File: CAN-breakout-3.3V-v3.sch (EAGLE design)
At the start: 11 parts, among them IC1 TJA1049

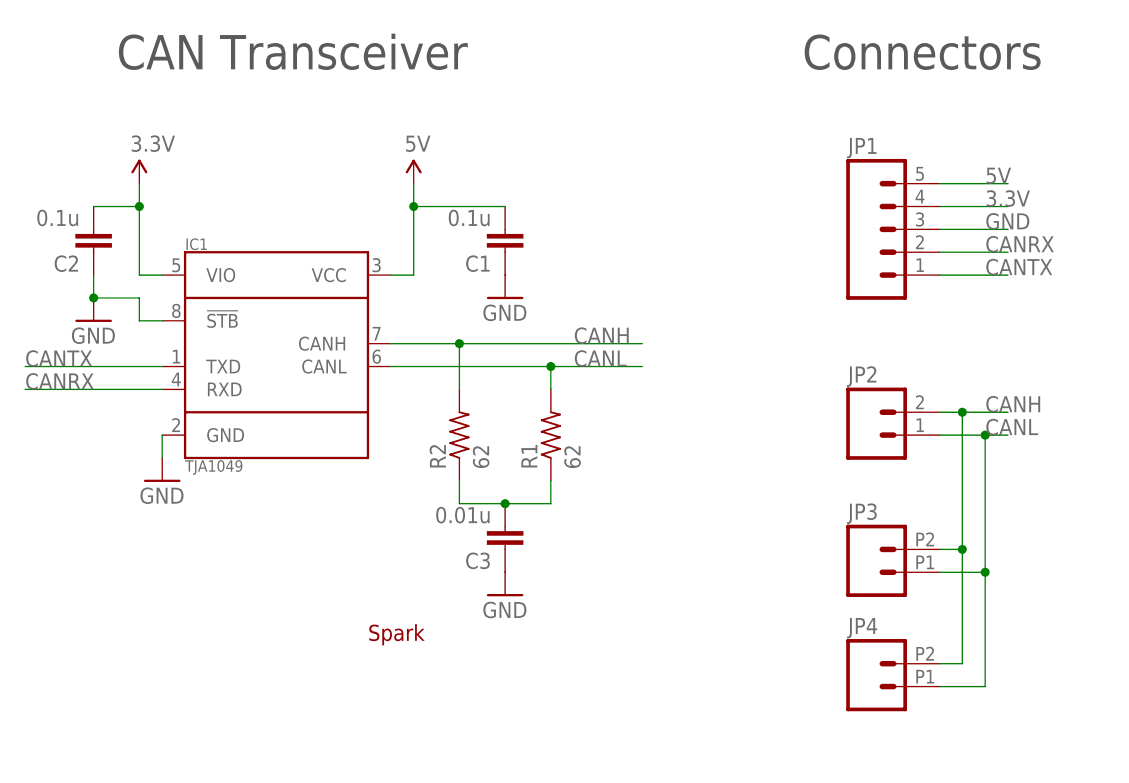
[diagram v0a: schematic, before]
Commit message: Add 3.3V variant
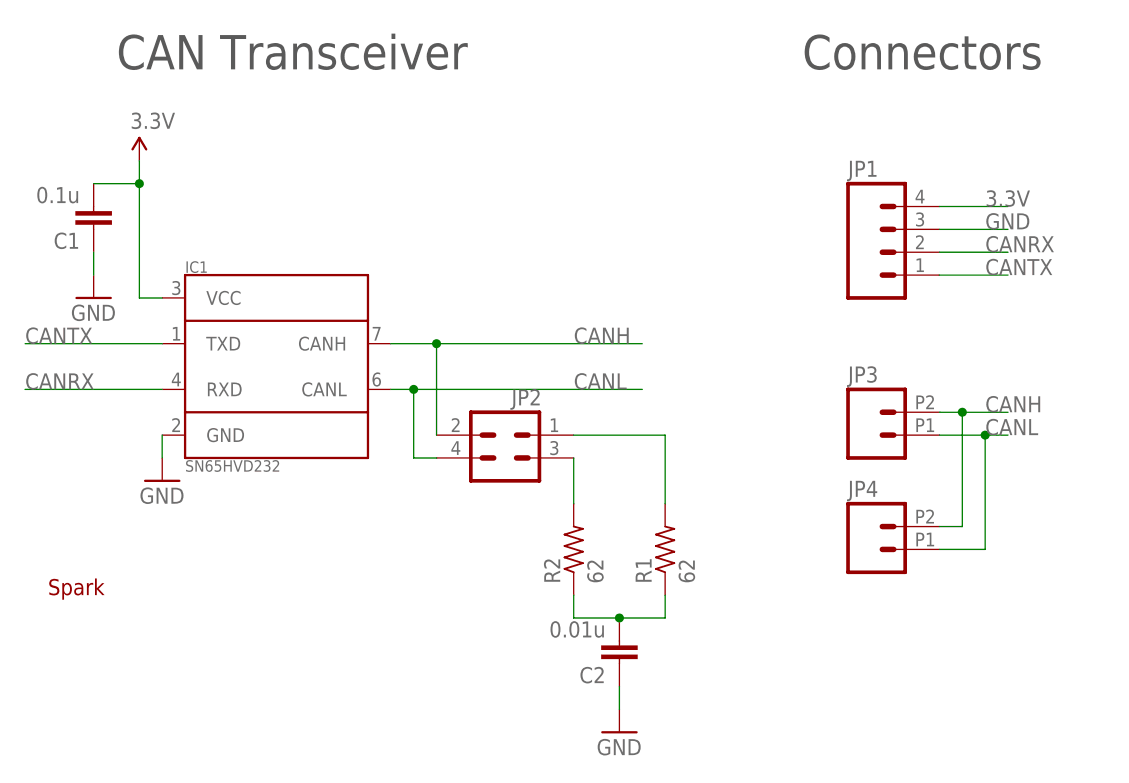
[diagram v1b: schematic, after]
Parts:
- removed C3: 0.01u, rcl:C-EUC1206
- C2: value 0.1u -> 0.01u; PARTNO 12065C104KAT2A -> 12065C103KAT2A
- IC1: value TJA1049 -> SN65HVD232; device CAN:TJA1049 -> CAN:SN65HVD232
- JP1: device SparkFun-Connectors:M05PTH -> SparkFun-Connectors:M04PTH
- JP2: device SparkFun-Connectors:M02PTH -> CAN:M02X2; PARTNO PREC002SAAN-RC -> (none)
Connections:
- removed net 5V: C1.2, IC1.VCC, JP1.5
- new net N$1: JP2.1, R1.2
- new net N$10: JP2.3, R2.2
- net 3.3V: now also C1.2, IC1.VCC; no longer C2.2, IC1.VIO
- net CANH: no longer R2.2
- net CANL: now also JP2.4; no longer JP2.1, R1.2
- net GND: no longer C3.1, IC1.!STB
- net N$7: now also C2.2; no longer C3.2
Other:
- moved on the sheet: C1, C2, JP3, JP4, R1, R2

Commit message: Create Gerbers
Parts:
- removed U$3: SPARK_LOGO2, Spark:SPARK_LOGO2
- IC1: PARTNO TJA1049T-118 -> SN65HVD232DR
- JP1: PARTNO PREC005SAAN-RC -> PREC004SAAN-RC
- JP2: PARTNO (none) -> PREC002DAAN-RC
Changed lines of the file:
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@@
 <grid distance="0.1" unitdist="inch" unit="inch" style="lines" multiple="1" display="no" altdistance="0.01" altunitdist="inch" altunit="inch"/>
 <layers>
-<layer number="1" name="Top" color="4" fill="1" visible="yes" active="no"/>
-<layer number="2" name="Route2" color="1" fill="3" visible="yes" active="no"/>
-<layer number="3" name="Route3" color="4" fill="3" visible="yes" active="no"/>
-<layer number="4" name="Route4" color="1" fill="4" visible="yes" active="no"/>
-<layer number="5" name="Route5" color="4" fill="4" visible="yes" active="no"/>
-<layer number="6" name="Route6" color="1" fill="8" visible="yes" active="no"/>
-<layer number="7" name="Route7" color="4" fill="8" visible="yes" active="no"/>
-<layer number="8" name="Route8" color="1" fill="2" visible="yes" active="no"/>
-<layer number="9" name="Route9" color="4" fill="2" visible="yes" active="no"/>
-<layer number="10" name="Route10" color="1" fill="7" visible="yes" active="no"/>
-<layer number="11" name="Route11" color="4" fill="7" visible="yes" active="no"/>
-<layer number="12" name="Route12" color="1" fill="5" visible="yes" active="no"/>
-<layer number="13" name="Route13" color="4" fill="5" visible="yes" active="no"/>
-<layer number="14" name="Route14" color="1" fill="6" visible="yes" active="no"/>
-<layer number="15" name="Route15" color="4" fill="6" visible="yes" active="no"/>
-<layer number="16" name="Bottom" color="1" fill="1" visible="yes" active="no"/>
-<layer number="17" name="Pads" color="2" fill="1" visible="yes" active="no"/>
-<layer number="18" name="Vias" color="2" fill="1" visible="yes" active="no"/>
-<layer number="19" name="Unrouted" color="6" fill="1" visible="yes" active="no"/>
-<layer number="20" name="Dimension" color="15" fill="1" visible="yes" active="no"/>
-<layer number="21" name="tPlace" color="7" fill="1" visible="yes" active="no"/>
-<layer number="22" name="bPlace" color="7" fill="1" visible="yes" active="no"/>
-<layer number="23" name="tOrigins" color="15" fill="1" visible="yes" active="no"/>
-<layer number="24" name="bOrigins" color="15" fill="1" visible="yes" active="no"/>
-<layer number="25" name="tNames" color="7" fill="1" visible="yes" active="no"/>
-<layer number="26" name="bNames" color="7" fill="1" visible="yes" active="no"/>
-<layer number="27" name="tValues" color="7" fill="1" visible="yes" active="no"/>
-<layer number="28" name="bValues" color="7" fill="1" visible="yes" active="no"/>
+<layer number="1" name="Top" color="4" fill="1" visible="no" active="no"/>
+<layer number="2" name="Route2" color="1" fill="3" visible="no" active="no"/>
+<layer number="3" name="Route3" color="4" fill="3" visible="no" active="no"/>
+<layer number="4" name="Route4" color="1" fill="4" visible="no" active="no"/>
+<layer number="5" name="Route5" color="4" fill="4" visible="no" active="no"/>
+<layer number="6" name="Route6" color="1" fill="8" visible="no" active="no"/>
+<layer number="7" name="Route7" color="4" fill="8" visible="no" active="no"/>
+<layer number="8" name="Route8" color="1" fill="2" visible="no" active="no"/>
+<layer number="9" name="Route9" color="4" fill="2" visible="no" active="no"/>
+<layer number="10" name="Route10" color="1" fill="7" visible="no" active="no"/>
+<layer number="11" name="Route11" color="4" fill="7" visible="no" active="no"/>
+<layer number="12" name="Route12" color="1" fill="5" visible="no" active="no"/>
+<layer number="13" name="Route13" color="4" fill="5" visible="no" active="no"/>
+<layer number="14" name="Route14" color="1" fill="6" visible="no" active="no"/>
+<layer number="15" name="Route15" color="4" fill="6" visible="no" active="no"/>
+<layer number="16" name="Bottom" color="1" fill="1" visible="no" active="no"/>
+<layer number="17" name="Pads" color="2" fill="1" visible="no" active="no"/>
+<layer number="18" name="Vias" color="2" fill="1" visible="no" active="no"/>
+<layer number="19" name="Unrouted" color="6" fill="1" visible="no" active="no"/>
+<layer number="20" name="Dimension" color="15" fill="1" visible="no" active="no"/>
+<layer number="21" name="tPlace" color="7" fill="1" visible="no" active="no"/>
+<layer number="22" name="bPlace" color="7" fill="1" visible="no" active="no"/>
+<layer number="23" name="tOrigins" color="15" fill="1" visible="no" active="no"/>
+<layer number="24" name="bOrigins" color="15" fill="1" visible="no" active="no"/>
+<layer number="25" name="tNames" color="7" fill="1" visible="no" active="no"/>
+<layer number="26" name="bNames" color="7" fill="1" visible="no" active="no"/>
+<layer number="27" name="tValues" color="7" fill="1" visible="no" active="no"/>
+<layer number="28" name="bValues" color="7" fill="1" visible="no" active="no"/>
 <layer number="29" name="tStop" color="7" fill="3" visible="no" active="no"/>
 <layer number="30" name="bStop" color="7" fill="6" visible="no" active="no"/>
@@
 <layer number="35" name="tGlue" color="7" fill="4" visible="no" active="no"/>
 <layer number="36" name="bGlue" color="7" fill="5" visible="no" active="no"/>
-<layer number="37" name="tTest" color="7" fill="1" visible="yes" active="no"/>
-<layer number="38" name="bTest" color="7" fill="1" visible="yes" active="no"/>
+<layer number="37" name="tTest" color="7" fill="1" visible="no" active="no"/>
+<layer number="38" name="bTest" color="7" fill="1" visible="no" active="no"/>
 <layer number="39" name="tKeepout" color="4" fill="11" visible="no" active="no"/>
 <layer number="40" name="bKeepout" color="1" fill="11" visible="no" active="no"/>
@@
 <layer number="44" name="Drills" color="7" fill="1" visible="no" active="no"/>
 <layer number="45" name="Holes" color="7" fill="1" visible="no" active="no"/>
-<layer number="46" name="Milling" color="3" fill="1" visible="yes" active="no"/>
-<layer number="47" name="Measures" color="7" fill="1" visible="yes" active="no"/>
-<layer number="48" name="Document" color="7" fill="1" visible="yes" active="no"/>
-<layer number="49" name="Reference" color="7" fill="1" visible="yes" active="no"/>
-<layer number="50" name="dxf" color="7" fill="1" visible="yes" active="no"/>
-<layer number="51" name="tDocu" color="7" fill="1" visible="yes" active="no"/>
-<layer number="52" name="bDocu" color="7" fill="1" visible="yes" active="no"/>
-<layer number="53" name="tGND_GNDA" color="7" fill="9" visible="yes" active="no"/>
-<layer number="54" name="bGND_GNDA" color="1" fill="9" visible="yes" active="no"/>
-<layer number="56" name="wert" color="7" fill="1" visible="yes" active="no"/>
-<layer number="57" name="tCAD" color="7" fill="1" visible="yes" active="no"/>
-<layer number="59" name="tCarbon" color="7" fill="1" visible="yes" active="no"/>
-<layer number="60" name="bCarbon" color="7" fill="1" visible="yes" active="no"/>
+<layer number="46" name="Milling" color="3" fill="1" visible="no" active="no"/>
+<layer number="47" name="Measures" color="7" fill="1" visible="no" active="no"/>
+<layer number="48" name="Document" color="7" fill="1" visible="no" active="no"/>
+<layer number="49" name="Reference" color="7" fill="1" visible="no" active="no"/>
+<layer number="50" name="dxf" color="7" fill="1" visible="no" active="no"/>
+<layer number="51" name="tDocu" color="7" fill="1" visible="no" active="no"/>
+<layer number="52" name="bDocu" color="7" fill="1" visible="no" active="no"/>
+<layer number="53" name="tGND_GNDA" color="7" fill="9" visible="no" active="no"/>
+<layer number="54" name="bGND_GNDA" color="1" fill="9" visible="no" active="no"/>
+<layer number="56" name="wert" color="7" fill="1" visible="no" active="no"/>
+<layer number="57" name="tCAD" color="7" fill="1" visible="no" active="no"/>
+<layer number="59" name="tCarbon" color="7" fill="1" visible="no" active="no"/>
+<layer number="60" name="bCarbon" color="7" fill="1" visible="no" active="no"/>
 <layer number="90" name="Modules" color="5" fill="1" visible="yes" active="yes"/>
 <layer number="91" name="Nets" color="2" fill="1" visible="yes" active="yes"/>
@@
 <part name="GND15" library="SparkFun-Aesthetics" deviceset="GND" device=""/>
 <part name="IC1" library="CAN" deviceset="SN65HVD232" device="">
-<attribute name="PARTNO" value="TJA1049T-118"/>
+<attribute name="PARTNO" value="SN65HVD232DR"/>
 </part>
 <part name="R2" library="rcl" deviceset="R-US_" device="R1206" value="62">
@@
 <part name="GND2" library="SparkFun-Aesthetics" deviceset="GND" device=""/>
 <part name="JP1" library="SparkFun-Connectors" deviceset="M04" device="PTH">
-<attribute name="PARTNO" value="PREC005SAAN-RC"/>
+<attribute name="PARTNO" value="PREC004SAAN-RC"/>
 </part>
 <part name="JP3" library="SparkFun-Connectors" deviceset="M02" device="2.54MM_SCREWTERM">
@@
 <attribute name="PARTNO" value="OSTVN02A150"/>
 </part>
-<part name="U$3" library="Spark" deviceset="SPARK_LOGO2" device="">
-<attribute name="BOM" value="EXCLUDE"/>
-</part>
 <part name="C2" library="rcl" deviceset="C-EU" device="C1206" value="0.01u">
 <attribute name="PARTNO" value="12065C103KAT2A"/>
 </part>
-<part name="JP2" library="CAN" deviceset="M02X2" device=""/>
+<part name="JP2" library="CAN" deviceset="M02X2" device="">
+<attribute name="PARTNO" value="PREC002DAAN-RC"/>
+</part>
+<part name="JP1-ALT" library="bom" deviceset="BOM-ENTRY" device="">
+<attribute name="PARTNO" value="PEC04SBBN"/>
+</part>
 </parts>
 <sheets>
@@
 <attribute name="PARTNO" x="157.48" y="101.6" size="1.778" layer="96" display="off"/>
 </instance>
-<instance part="U$3" gate="G$1" x="66.04" y="96.52">
-<attribute name="BOM" x="66.04" y="96.52" size="1.778" layer="96" display="off"/>
-</instance>
 <instance part="C2" gate="G$1" x="129.54" y="88.9" rot="R180">
 <attribute name="PARTNO" x="129.54" y="88.9" size="1.778" layer="96" rot="R90" display="off"/>
 </instance>
-<instance part="JP2" gate="G$1" x="116.84" y="111.76" rot="MR0"/>
+<instance part="JP2" gate="G$1" x="116.84" y="111.76" rot="MR0">
+<attribute name="PARTNO" x="116.84" y="111.76" size="1.778" layer="96" display="off"/>
+</instance>
+<instance part="JP1-ALT" gate="G$1" x="154.94" y="91.44"/>
 </instances>
 <busses>
